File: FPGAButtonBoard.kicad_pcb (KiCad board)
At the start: 2 copper layers, 121.3 x 83.2 mm, 66 parts, among them J1 Conn_02x20_Odd_Even, J2 Analog Discovery 2, SW1 SW_DIP_x08, SW2 SW_DIP_x08, SW3 SW_Push, SW4 SW_Push, SW5 SW_Push, SW6 SW_Push, SW7 SW_Push, SW8 SW_Push_DPDT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

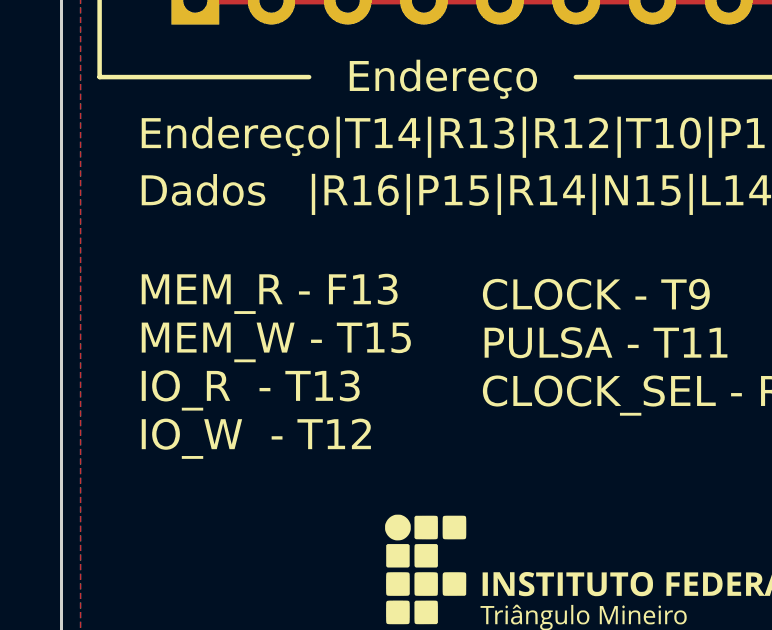
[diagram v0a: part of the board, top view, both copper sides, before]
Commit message: Corrigido um erro no silkscren. Opino do MEM_R está invertido com o MEM_W
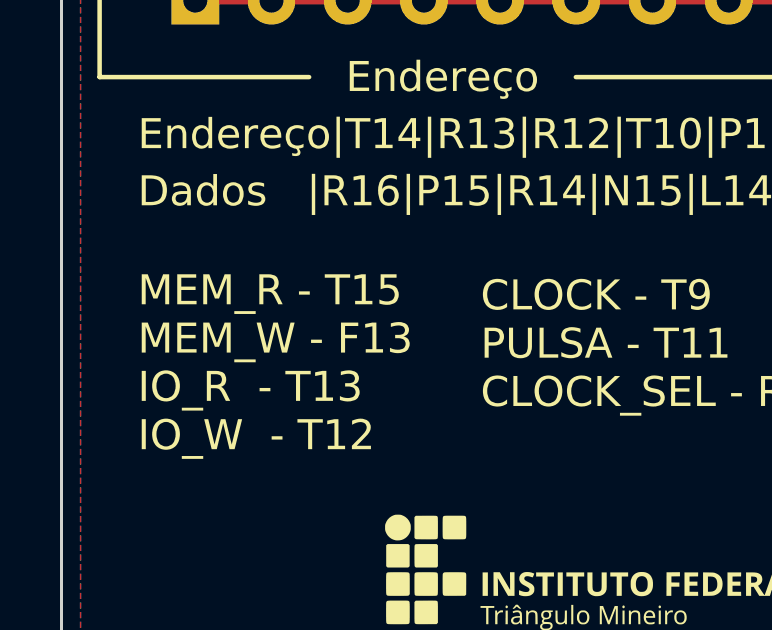
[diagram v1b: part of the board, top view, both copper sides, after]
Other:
- board text added: "MEM_R - T15 MEM_W - F13 IO_R - T13 IO_W - T12"
- board text removed: "MEM_R - F13 MEM_W - T15 IO_R - T13 IO_W - T12"
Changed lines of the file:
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@@
     (effects (font (size 1 1) (thickness 0.15)))
   )
-  (gr_text "MEM_R - F13\nMEM_W - T15\nIO_R  - T13\nIO_W  - T12\n" (at 92.71 121.285) (layer "F.SilkS")
+  (gr_text "MEM_R - T15\nMEM_W - F13\nIO_R  - T13\nIO_W  - T12\n" (at 92.71 121.285) (layer "F.SilkS")
     (effects (font (size 1 1) (thickness 0.15)) (justify left))
   )
